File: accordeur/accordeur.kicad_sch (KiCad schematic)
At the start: 36 parts, among them Q1 2N3904, SW1 SW_DPDT_x2, SW2 SW_DPDT_x2, U1 LM358, U2 LM358, U3 LM339

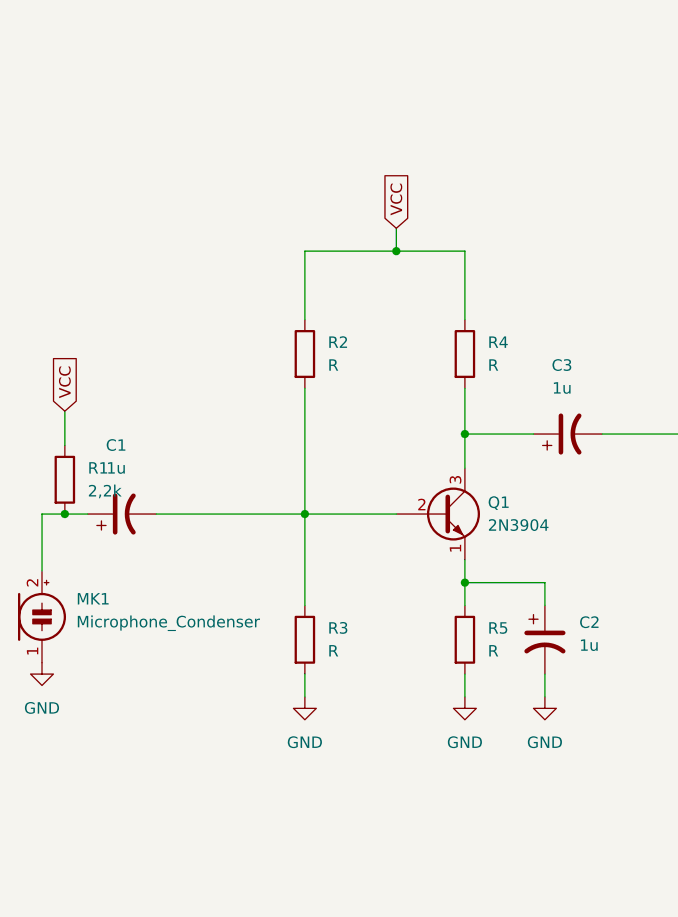
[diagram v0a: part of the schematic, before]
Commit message: Changements de Emz
Ajout de quelques footprints
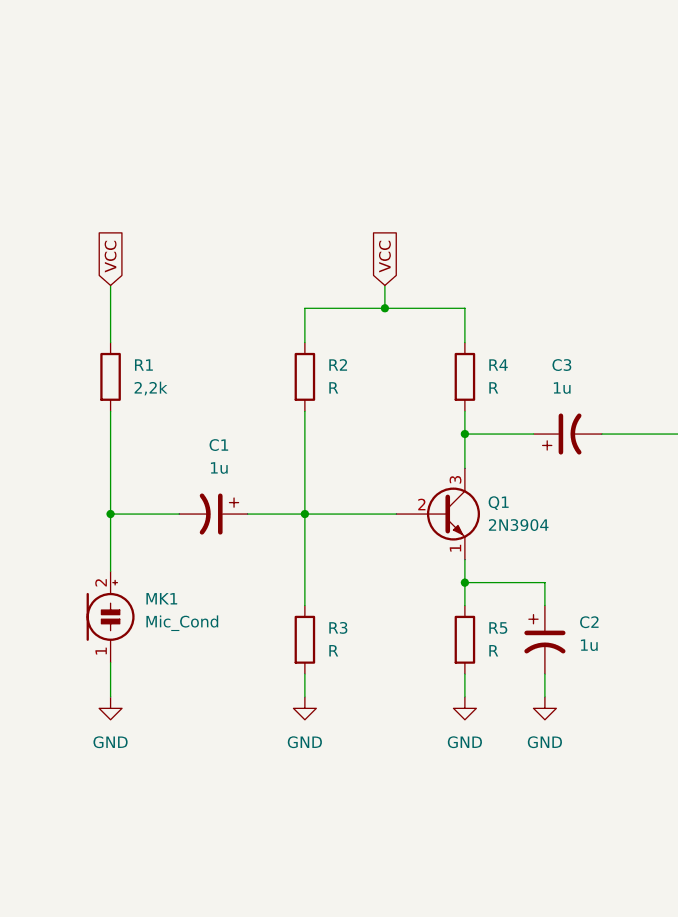
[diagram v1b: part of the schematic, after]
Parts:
- D5, D6, D7, D8: footprint (none) -> LED:LED_151054RS03000
- MK1: value Microphone_Condenser -> Mic_Cond; footprint (none) -> MIC:MIC_CMA-4544PF-W
- R1, R10, R11, R12, R13, R2, R3, R4, R5, R6, R7, R8, R9: footprint (none) -> Resistor_SMD:R_0805_2012Metric
- RV1: footprint (none) -> POT:POT_3299W-1-104LF
- SW1, SW2: footprint (none) -> SWITCH:SW_100AWDP1T2B4M2QE
- U2: footprint (none) -> Package_DIP:DIP-8_W7.62mm
- U3: footprint (none) -> Package_DIP:DIP-16_W7.62mm
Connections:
- net at Q1.2 (B), R2.2, R3.1: now also C1.1; no longer C1.2
- net at MK1.2 (+), R1.2: now also C1.2; no longer C1.1
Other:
- moved on the sheet: C1, MK1, R1, R2, R4

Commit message: Finalisation de la rev 0 du PCB
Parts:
- removed SW1, SW2: SW_DPDT_x2, SWITCH:SW_100AWDP1T2B4M2QE, symbol Switch:SW_DPDT_x2
- added J1: Screw_Terminal_01x03, TerminalBlock:TerminalBlock_bornier-3_P5.08mm, symbol Connector:Screw_Terminal_01x03
- added SW1: SW_SPST, SWITCH:A11AP, symbol Switch:SW_SPST
- C1, C2, C3, C4, C5, C6, C7: footprint (none) -> Capacitor_THT:CP_Radial_D5.0mm_P2.50mm
- D1, D2, D3, D4: footprint (none) -> Diode_SMD:D_0805_2012Metric
- D5, D6, D7, D8: footprint LED:LED_151054RS03000 -> LED_THT:LED_D5.0mm
- RV1: value R_Potentiometer -> 100k; footprint POT:POT_3299W-1-104LF -> POT:POT_emz_marc
- U3: footprint Package_DIP:DIP-16_W7.62mm -> Package_DIP:DIP-14_W7.62mm
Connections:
- net GND: now also U3.12 (V-), J1.2 (Pin_2)
- net PB A3/v_sig: now also SW1.2 (B)
- net at C3.2: now also SW1.1 (A)
- net VCC renamed +5V
- net +5V: now also J1.1 (Pin_1)
- net VEE renamed -5V
- net -5V: now also J1.3 (Pin_3); no longer U3.12 (V-)
- no-connect marks 4 -> 0
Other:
- moved on the sheet: C1, C2, C3, MK1, Q1, R1, R2, R3, R4, R5, RV1

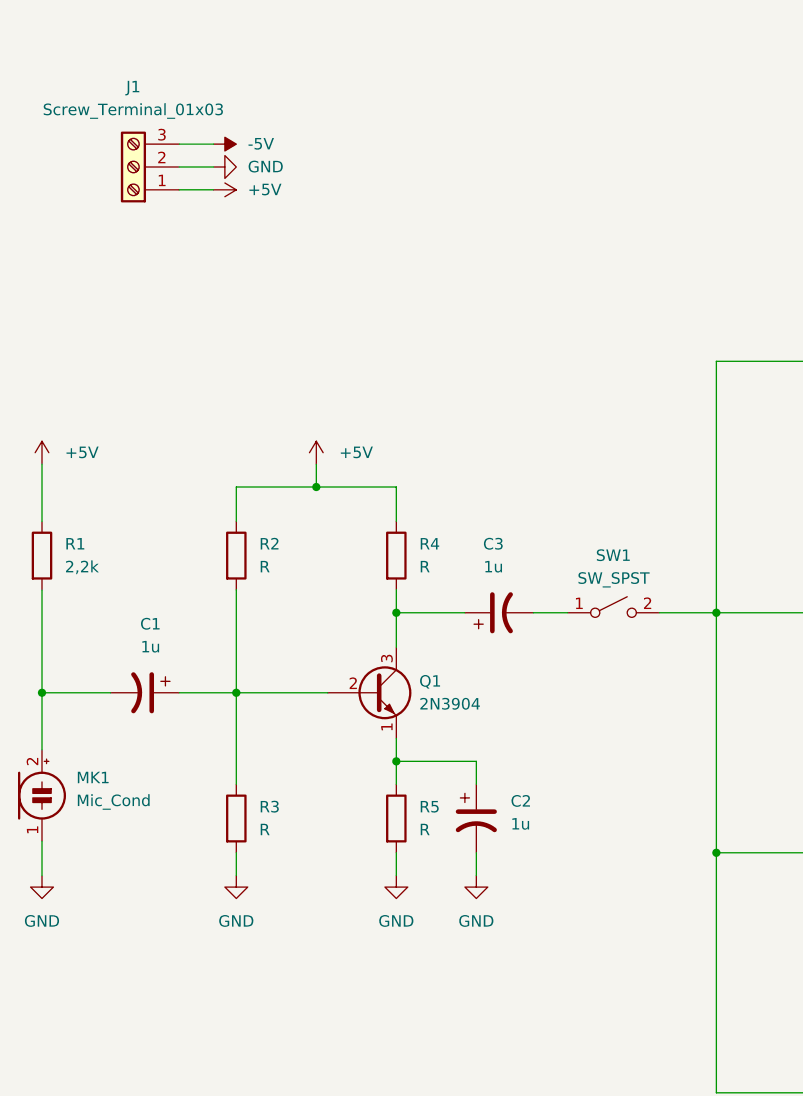
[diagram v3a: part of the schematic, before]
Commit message: Finalisation du placement des pièces
Prochaine étape : routing
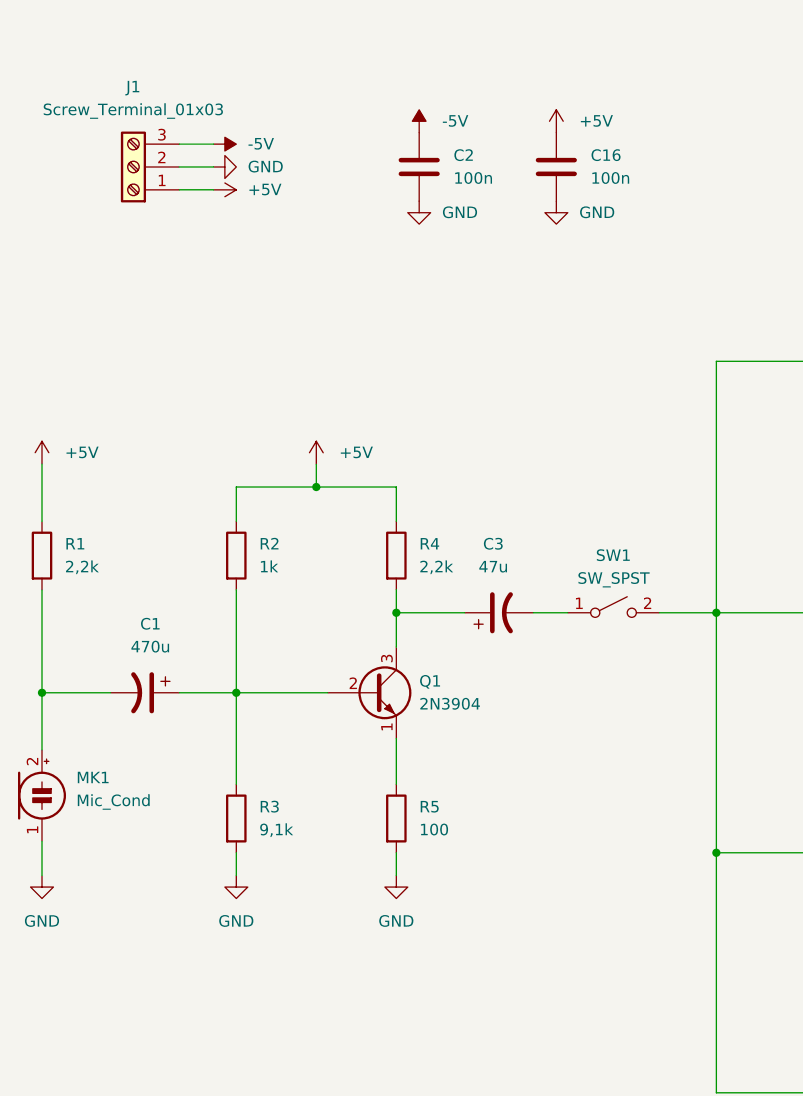
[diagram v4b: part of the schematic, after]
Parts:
- removed C2: 1u, Capacitor_THT:CP_Radial_D5.0mm_P2.50mm, symbol Device:C_Polarized_US
- added C16, C2: 100n, Capacitor_SMD:C_0805_2012Metric_Pad1.18x1.45mm_HandSolder, symbol Device:C
- C1: value 1u -> 470u; footprint Capacitor_THT:CP_Radial_D5.0mm_P2.50mm -> Capacitor_THT:CP_Radial_D7.5mm_P2.50mm
- C3: value 1u -> 47u
- D1, D2, D3, D4: footprint Diode_SMD:D_0805_2012Metric -> Diode_SMD:D_0805_2012Metric_Pad1.15x1.40mm_HandSolder
- R1, R10, R11, R12, R13, R6, R7, R8, R9: footprint Resistor_SMD:R_0805_2012Metric -> Resistor_SMD:R_0805_2012Metric_Pad1.20x1.40mm_HandSolder
- R2: value R -> 1k; footprint Resistor_SMD:R_0805_2012Metric -> Resistor_SMD:R_0805_2012Metric_Pad1.20x1.40mm_HandSolder
- R3: value R -> 9,1k; footprint Resistor_SMD:R_0805_2012Metric -> Resistor_SMD:R_0805_2012Metric_Pad1.20x1.40mm_HandSolder
- R4: value R -> 2,2k; footprint Resistor_SMD:R_0805_2012Metric -> Resistor_SMD:R_0805_2012Metric_Pad1.20x1.40mm_HandSolder
- R5: value R -> 100; footprint Resistor_SMD:R_0805_2012Metric -> Resistor_SMD:R_0805_2012Metric_Pad1.20x1.40mm_HandSolder
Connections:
- net +5V: now also C16.1
- net -5V: now also C2.1
- net GND: now also C16.2, C2.2

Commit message: PCB commandé
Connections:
- net -5V: now also R3.2, R5.2
- net GND: no longer R3.2, R5.2
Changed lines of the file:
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@@
     (pin "9")
+  )
+  (symbol (lib_id "power:-5V") (at 46.99 109.22 180) (unit 1)
+    (in_bom yes) (on_board yes) (fields_autoplaced)
+    (property "Reference" "#PWR0109" (id 0) (at 46.99 111.76 0)
+      (effects (font (size 1.27 1.27)) hide)
+    )
+    (property "Value" "-5V" (id 1) (at 49.53 110.4899 0)
+      (effects (font (size 1.27 1.27)) (justify right))
+    )
+    (property "Footprint" "" (id 2) (at 46.99 109.22 0)
+      (effects (font (size 1.27 1.27)) hide)
+    )
+    (property "Datasheet" "" (id 3) (at 46.99 109.22 0)
+      (effects (font (size 1.27 1.27)) hide)
+    )
+    (pin "1")
   )
   (symbol (lib_id "Switch:SW_SPST") (at 88.9 80.01 0) (unit 1)
@@
     (pin "2")
   )
-  (symbol (lib_id "power:GND") (at 64.77 109.22 0) (unit 1)
-    (in_bom yes) (on_board yes) (fields_autoplaced)
-    (property "Reference" "#PWR03" (id 0) (at 64.77 115.57 0)
-      (effects (font (size 1.27 1.27)) hide)
-    )
-    (property "Value" "GND" (id 1) (at 64.77 114.3 0))
+  (symbol (lib_id "power:-5V") (at 64.77 109.22 180) (unit 1)
+    (in_bom yes) (on_board yes) (fields_autoplaced)
+    (property "Reference" "#PWR0110" (id 0) (at 64.77 111.76 0)
+      (effects (font (size 1.27 1.27)) hide)
+    )
+    (property "Value" "-5V" (id 1) (at 67.31 110.4899 0)
+      (effects (font (size 1.27 1.27)) (justify right))
+    )
     (property "Footprint" "" (id 2) (at 64.77 109.22 0)
       (effects (font (size 1.27 1.27)) hide)
@@
     (pin "2")
     (pin "3")
-  )
-  (symbol (lib_id "power:GND") (at 46.99 109.22 0) (unit 1)
-    (in_bom yes) (on_board yes) (fields_autoplaced)
-    (property "Reference" "#PWR02" (id 0) (at 46.99 115.57 0)
-      (effects (font (size 1.27 1.27)) hide)
-    )
-    (property "Value" "GND" (id 1) (at 46.99 114.3 0))
-    (property "Footprint" "" (id 2) (at 46.99 109.22 0)
-      (effects (font (size 1.27 1.27)) hide)
-    )
-    (property "Datasheet" "" (id 3) (at 46.99 109.22 0)
-      (effects (font (size 1.27 1.27)) hide)
-    )
-    (pin "1")
   )
   (symbol (lib_id "power:GND") (at 204.47 119.38 0) (unit 1)
@@
       (reference "#PWR01") (unit 1) (value "GND") (footprint "")
     )
-    (path "/ca99aeac-b449-4077-a4f4-098287128251"
-      (reference "#PWR02") (unit 1) (value "GND") (footprint "")
-    )
-    (path "/c33ab92d-bc03-4b63-8044-01a5b01349ad"
-      (reference "#PWR03") (unit 1) (value "GND") (footprint "")
-    )
     (path "/eaa60bd3-3fe7-4968-bff3-896b9934b3be"
       (reference "#PWR04") (unit 1) (value "-5V") (footprint "")
@@
       (reference "#PWR0108") (unit 1) (value "GND") (footprint "")
     )
+    (path "/b0813dc4-dc82-49ff-81b0-cb5e56980f48"
+      (reference "#PWR0109") (unit 1) (value "-5V") (footprint "")
+    )
+    (path "/c33a6e1b-e03e-4651-a513-e964d0848eeb"
+      (reference "#PWR0110") (unit 1) (value "-5V") (footprint "")
+    )
     (path "/33177557-ffe9-4faf-b534-adbfc313fdf1"
